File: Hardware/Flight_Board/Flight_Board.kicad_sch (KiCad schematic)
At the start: 0 parts

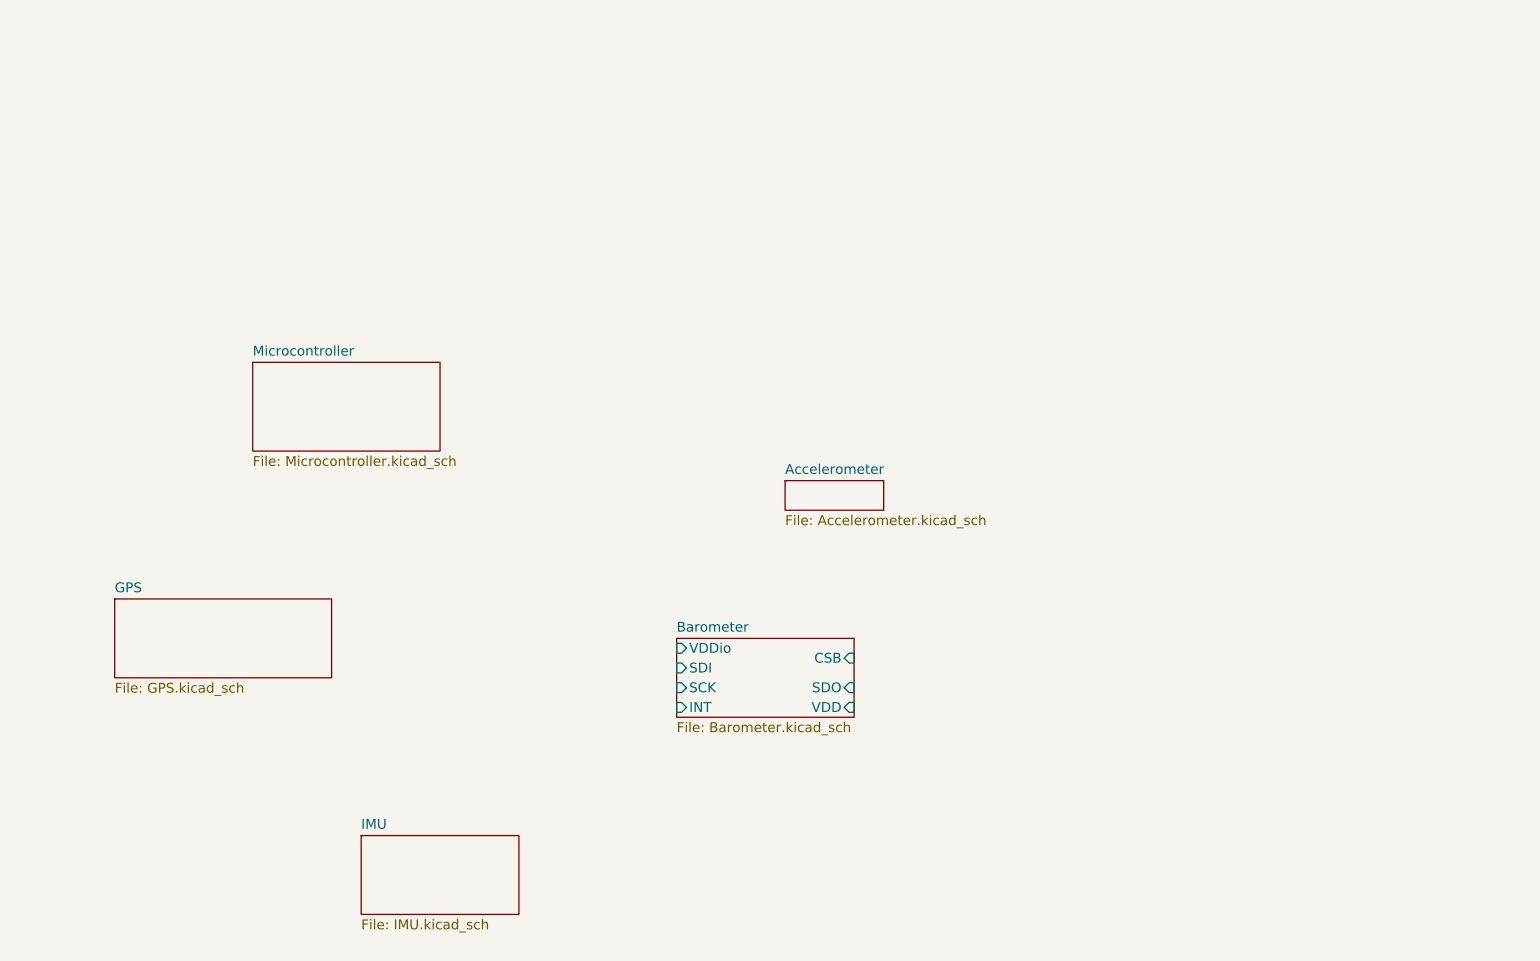
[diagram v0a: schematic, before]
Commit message: standardize connections and create initial spi2 bus
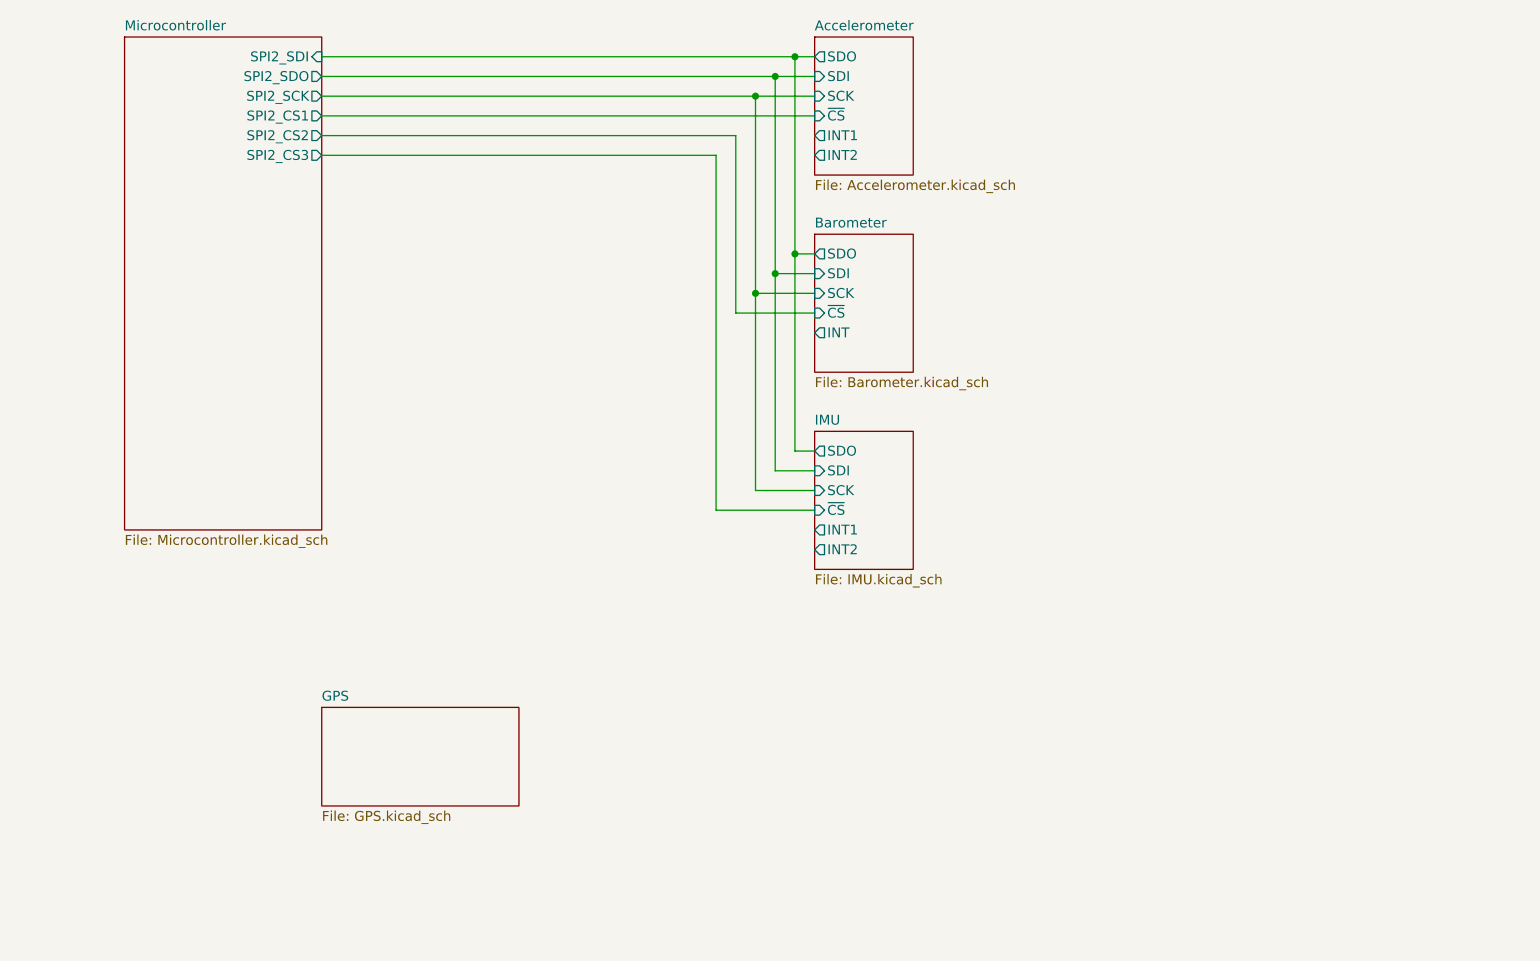
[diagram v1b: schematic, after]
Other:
- sheet Accelerometer ports: added INT1, INT2, SCK, SDI, SDO, ~{CS}; removed none
- sheet Barometer ports: added ~{CS}; removed CSB, VDD, VDDio
- sheet IMU ports: added INT1, INT2, SCK, SDI, SDO, ~{CS}; removed none
- sheet Microcontroller ports: added SPI2_CS1, SPI2_CS2, SPI2_CS3, SPI2_SCK, SPI2_SDI, SPI2_SDO; removed none

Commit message: Make GPS
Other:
- sheet GPS ports: added DSEL, EXTINT, RXD, SCL, SDA, TXD; removed none
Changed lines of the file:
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@@
       (effects (font (size 1.27 1.27)) (justify left top))
+    )
+    (pin "RXD" bidirectional (at 119.38 111.76 90)
+      (effects (font (size 1.27 1.27)) (justify right))
+    )
+    (pin "TXD" bidirectional (at 121.92 111.76 90)
+      (effects (font (size 1.27 1.27)) (justify right))
+    )
+    (pin "DSEL" input (at 124.46 111.76 90)
+      (effects (font (size 1.27 1.27)) (justify right))
+    )
+    (pin "EXTINT" bidirectional (at 127 111.76 90)
+      (effects (font (size 1.27 1.27)) (justify right))
+    )
+    (pin "SCL" input (at 139.7 115.57 0)
+      (effects (font (size 1.27 1.27)) (justify right))
+    )
+    (pin "SDA" bidirectional (at 139.7 118.11 0)
+      (effects (font (size 1.27 1.27)) (justify right))
     )
     (instances

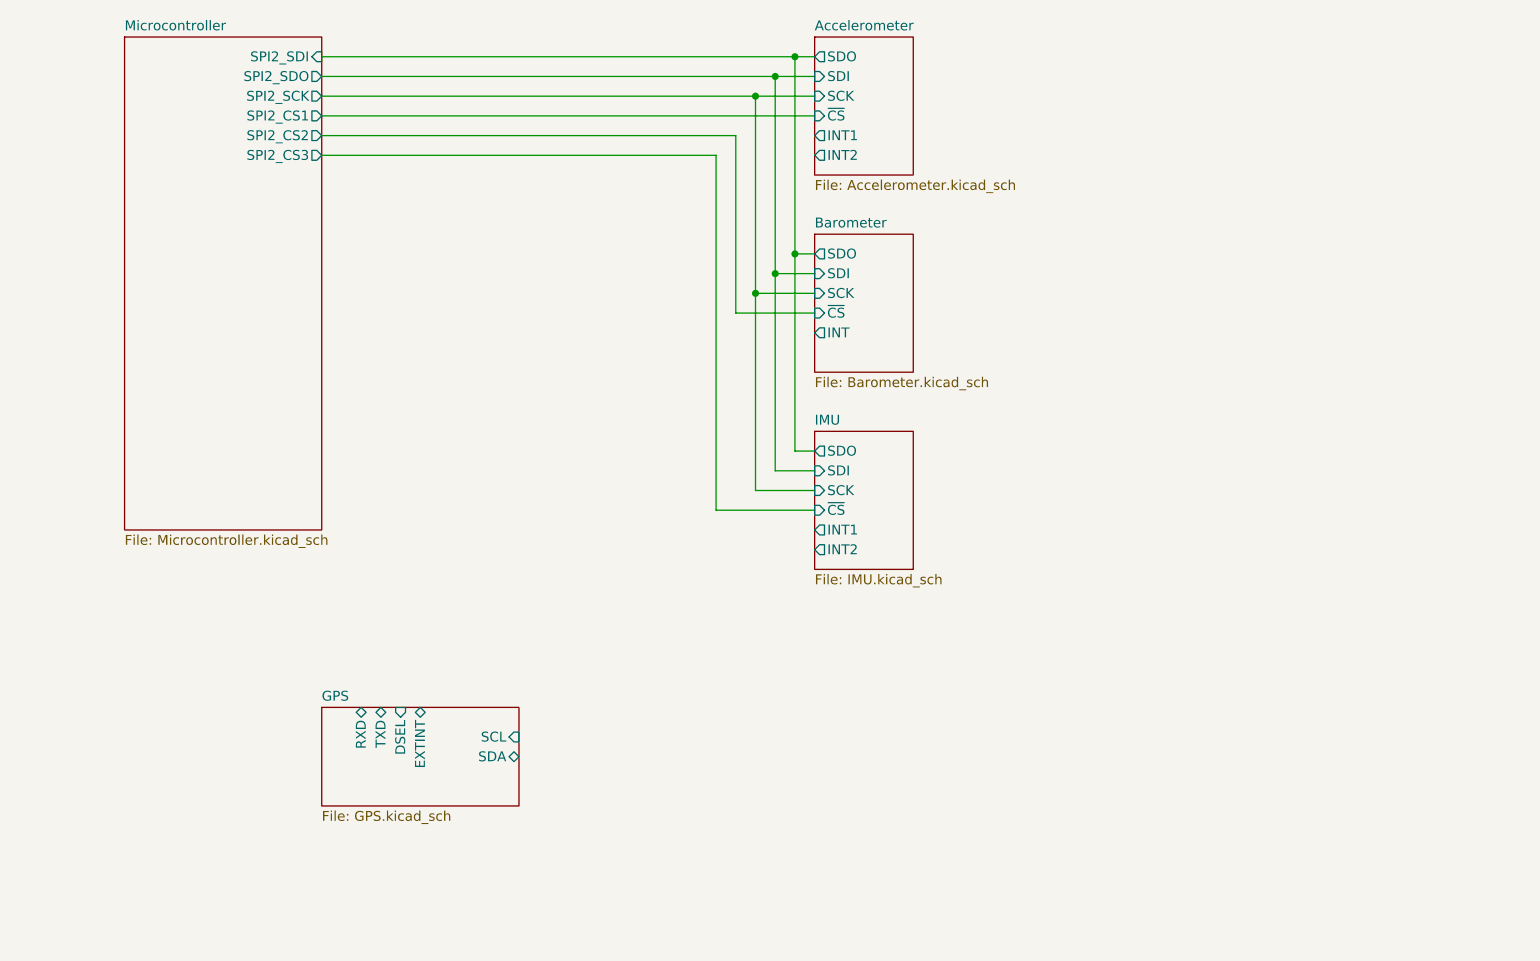
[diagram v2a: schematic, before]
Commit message: move ADLX375 to I2C, bring out more mcu pins, and general touchups
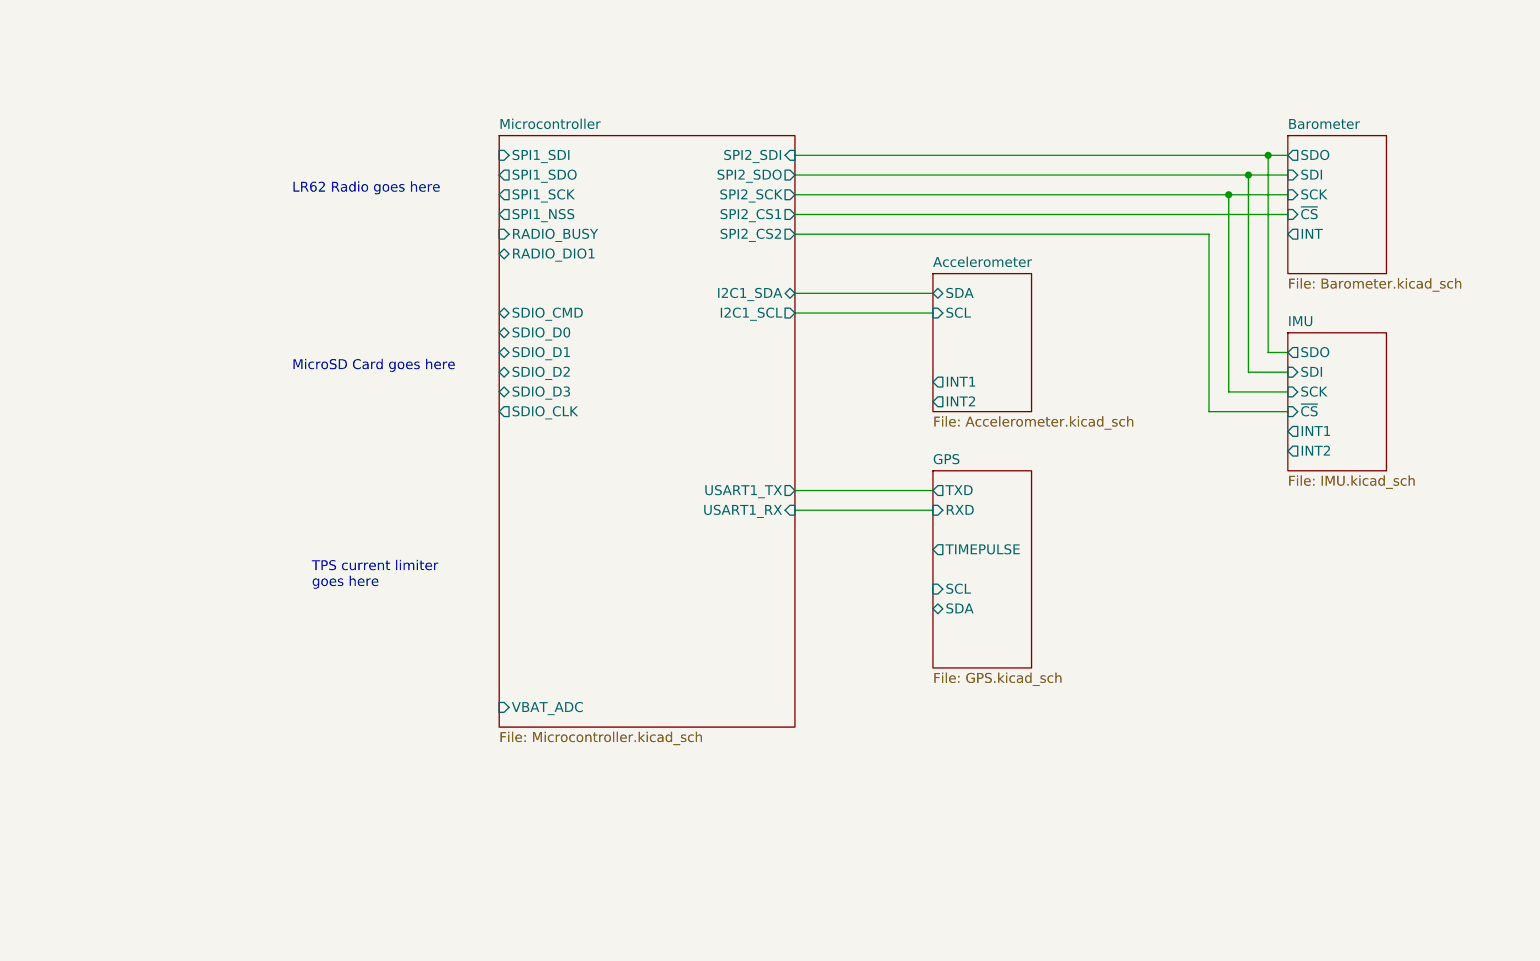
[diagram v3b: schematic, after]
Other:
- sheet Accelerometer ports: added SCL, SDA; removed SCK, SDI, SDO, ~{CS}
- sheet GPS ports: added TIMEPULSE; removed DSEL, EXTINT
- sheet Microcontroller ports: added I2C1_SCL, I2C1_SDA, RADIO_BUSY, RADIO_DIO1, SDIO_CLK, SDIO_CMD, SDIO_D0, SDIO_D1, SDIO_D2, SDIO_D3, SPI1_NSS, SPI1_SCK, SPI1_SDI, SPI1_SDO, USART1_RX, USART1_TX, VBAT_ADC; removed SPI2_CS3
- note added: "LR62 Radio goes here"
- note added: "MicroSD Card goes here"
- note added: "TPS current limiter goes here"

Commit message: Added Power Page
Power page added
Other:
- added sheet Power (Power.kicad_sch)
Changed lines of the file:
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@@
+    )
+  )
+  (sheet (at 74.93 128.27) (size 25.4 11.43) (fields_autoplaced)
+    (stroke (width 0.1524) (type solid))
+    (fill (color 0 0 0 0.0000))
+    (property "Sheetname" "Power" (at 74.93 127.5584 0)
+      (effects (font (size 1.27 1.27)) (justify left bottom))
+    )
+    (property "Sheetfile" "Power.kicad_sch" (at 74.93 140.2846 0)
+      (effects (font (size 1.27 1.27)) (justify left top))
+    )
+    (instances
+      (project "Flight_Board"
+        (path "/e8eb85d5-f1ff-4500-895d-25b9ff5f6d36" (page "7"))
+      )
     )
   )
